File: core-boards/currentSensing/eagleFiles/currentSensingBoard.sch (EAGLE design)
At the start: 22 parts, among them Q1 16MHz, X1 3-PIN_2MM-H, X2 2-PIN_2MM-H, X3 4-PIN_2MM-H

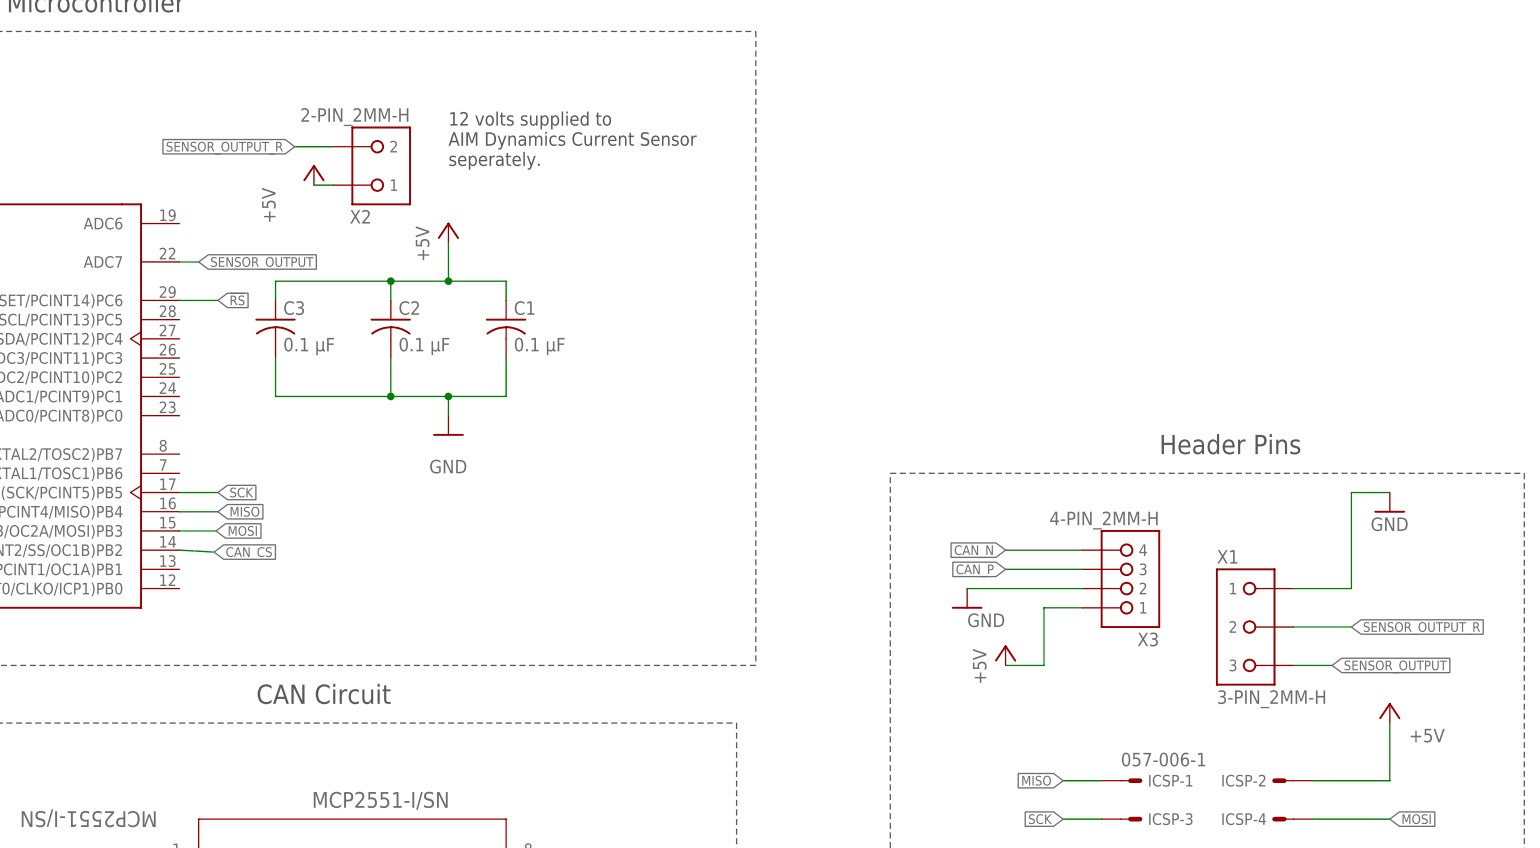
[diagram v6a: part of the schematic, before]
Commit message: SMD Resistor Update
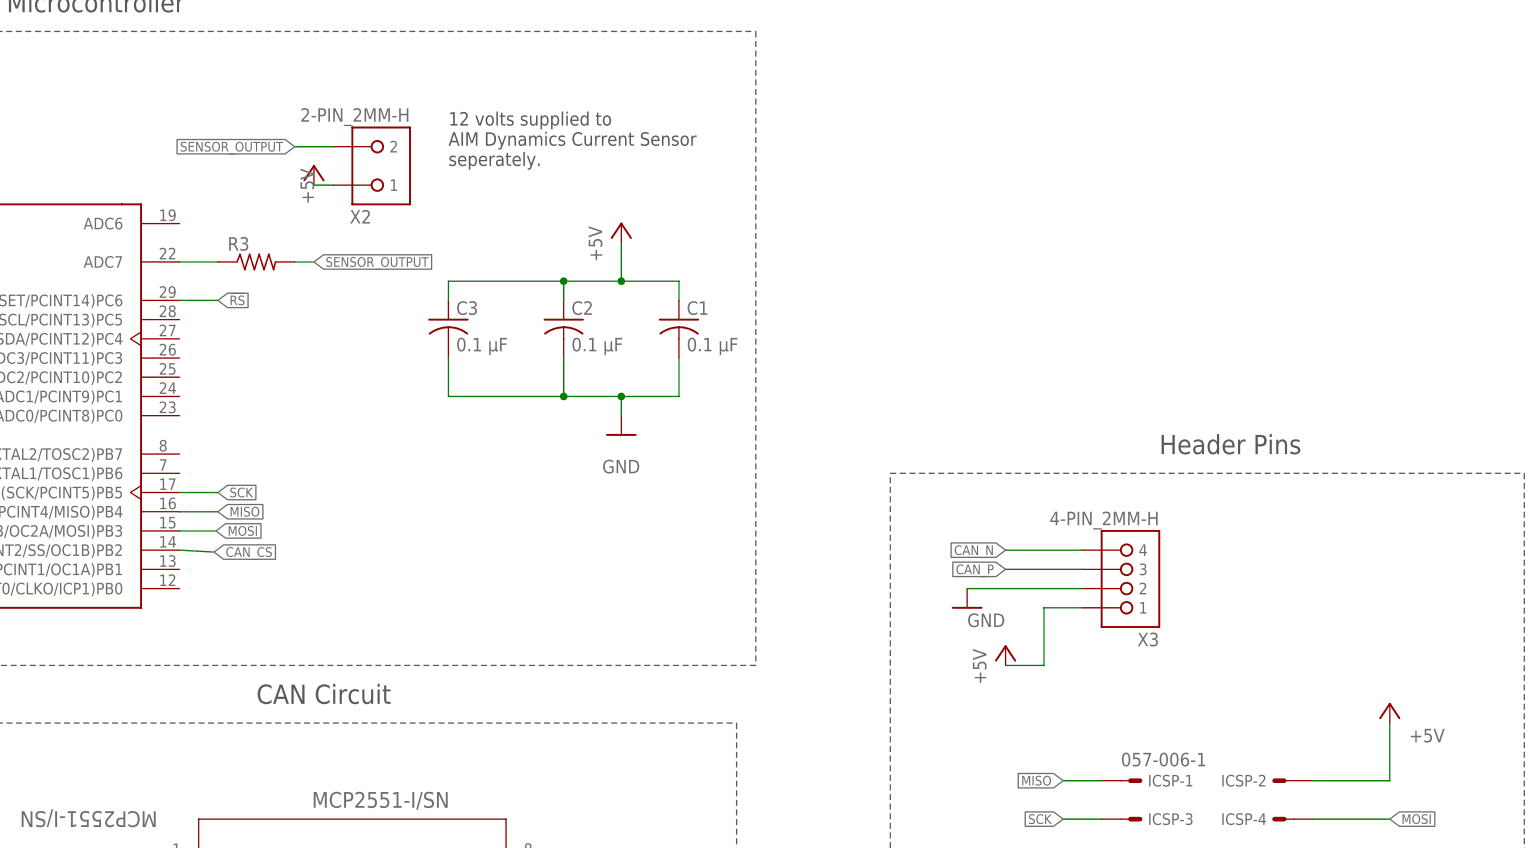
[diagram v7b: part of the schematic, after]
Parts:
- removed X1: 3-PIN_2MM-H, RoboJackets-Connectors:3-PIN_2MM-H
- added R3: (no value), RoboJackets-Resistors:R0603W
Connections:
- removed net SENSOR_OUTPUT_R: X1.2, X2.2
- new net N$2: ATMEGA328P-AU(V1).ADC7, R3.PIN1
- net GND: no longer X1.1
- net SENSOR_OUTPUT: now also R3.PIN2, X2.2; no longer ATMEGA328P-AU(V1).ADC7, X1.3
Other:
- moved on the sheet: C1, C2, C3
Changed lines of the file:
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@@
 <part name="R4" library="rcl" library_urn="urn:adsk.eagle:library:334" deviceset="R-US_" device="R0603" package3d_urn="urn:adsk.eagle:package:23555/3" value="120 Ω"/>
 <part name="R5" library="rcl" library_urn="urn:adsk.eagle:library:334" deviceset="R-US_" device="R0603" package3d_urn="urn:adsk.eagle:package:23555/3" value="120 Ω"/>
-<part name="X1" library="RoboJackets-Connectors" deviceset="3-PIN_2MM-*" device="H"/>
-<part name="GND5" library="supply1" library_urn="urn:adsk.eagle:library:371" deviceset="GND" device=""/>
 <part name="P+3" library="supply1" library_urn="urn:adsk.eagle:library:371" deviceset="+5V" device=""/>
 <part name="P+4" library="supply1" library_urn="urn:adsk.eagle:library:371" deviceset="+5V" device=""/>
@@
 <part name="DEBUG" library="RoboJackets-LEDs" deviceset="LED-SMD" device="" technology="-RED" value="RED"/>
 <part name="FRAME1" library="RoboJackets-Frames" deviceset="FRAME_B_L" device=""/>
+<part name="R3" library="RoboJackets-Resistors" deviceset="R0603W" device=""/>
 </parts>
 <sheets>
@@
 <attribute name="PARTS_NAME" x="147.32" y="215.9" size="1.778" layer="96"/>
 </instance>
-<instance part="C1" gate="G$1" x="233.68" y="198.12" smashed="yes">
-<attribute name="NAME" x="234.696" y="198.755" size="1.778" layer="95"/>
-<attribute name="VALUE" x="234.696" y="193.929" size="1.778" layer="96"/>
-</instance>
-<instance part="C2" gate="G$1" x="218.44" y="198.12" smashed="yes">
-<attribute name="NAME" x="219.456" y="198.755" size="1.778" layer="95"/>
-<attribute name="VALUE" x="219.456" y="193.929" size="1.778" layer="96"/>
-</instance>
-<instance part="P+1" gate="1" x="226.06" y="210.82" smashed="yes">
-<attribute name="VALUE" x="223.52" y="205.74" size="1.778" layer="96" rot="R90"/>
-</instance>
-<instance part="GND1" gate="1" x="226.06" y="182.88" smashed="yes">
-<attribute name="VALUE" x="223.52" y="177.8" size="1.778" layer="96"/>
+<instance part="C1" gate="G$1" x="256.54" y="198.12" smashed="yes">
+<attribute name="NAME" x="257.556" y="198.755" size="1.778" layer="95"/>
+<attribute name="VALUE" x="257.556" y="193.929" size="1.778" layer="96"/>
+</instance>
+<instance part="C2" gate="G$1" x="241.3" y="198.12" smashed="yes">
+<attribute name="NAME" x="242.316" y="198.755" size="1.778" layer="95"/>
+<attribute name="VALUE" x="242.316" y="193.929" size="1.778" layer="96"/>
+</instance>
+<instance part="P+1" gate="1" x="248.92" y="210.82" smashed="yes">
+<attribute name="VALUE" x="246.38" y="205.74" size="1.778" layer="96" rot="R90"/>
+</instance>
+<instance part="GND1" gate="1" x="248.92" y="182.88" smashed="yes">
+<attribute name="VALUE" x="246.38" y="177.8" size="1.778" layer="96"/>
 </instance>
 <instance part="GND2" gate="1" x="106.68" y="185.42" smashed="yes">
@@
 <attribute name="VALUE" x="254" y="119.38" size="1.778" layer="96"/>
 </instance>
-<instance part="C3" gate="G$1" x="203.2" y="198.12" smashed="yes">
-<attribute name="NAME" x="204.216" y="198.755" size="1.778" layer="95"/>
-<attribute name="VALUE" x="204.216" y="193.929" size="1.778" layer="96"/>
+<instance part="C3" gate="G$1" x="226.06" y="198.12" smashed="yes">
+<attribute name="NAME" x="227.076" y="198.755" size="1.778" layer="95"/>
+<attribute name="VALUE" x="227.076" y="193.929" size="1.778" layer="96"/>
 </instance>
 <instance part="C4" gate="G$1" x="116.84" y="187.96" smashed="yes" rot="R270">
@@
 <attribute name="VALUE" x="117.602" y="72.39" size="1.778" layer="96" rot="R90"/>
 </instance>
-<instance part="X1" gate="G$1" x="332.74" y="157.48" smashed="yes">
-<attribute name="NAME" x="327.66" y="167.64" size="1.778" layer="95" font="vector" align="top-left"/>
-<attribute name="VALUE" x="327.66" y="147.32" size="1.778" layer="96" font="vector"/>
-</instance>
-<instance part="GND5" gate="1" x="350.52" y="172.72" smashed="yes">
-<attribute name="VALUE" x="347.98" y="170.18" size="1.778" layer="96"/>
-</instance>
 <instance part="P+3" gate="1" x="101.6" y="218.44" smashed="yes">
 <attribute name="VALUE" x="99.06" y="213.36" size="1.778" layer="96" rot="R90"/>
@@
 </instance>
 <instance part="P+6" gate="1" x="208.28" y="218.44" smashed="yes">
-<attribute name="VALUE" x="203.2" y="210.82" size="1.778" layer="96" rot="R90"/>
+<attribute name="VALUE" x="208.28" y="213.36" size="1.778" layer="96" rot="R90"/>
 </instance>
 <instance part="GND7" gate="1" x="91.44" y="198.12" smashed="yes">
@@
 <attribute name="SCH_DESC" x="326.39" y="6.35" size="2.54" layer="94"/>
 </instance>
+<instance part="R3" gate="G$1" x="200.66" y="205.74" smashed="yes">
+<attribute name="NAME" x="196.85" y="207.2386" size="1.778" layer="95"/>
+<attribute name="VALUE" x="196.85" y="202.438" size="1.778" layer="96"/>
+</instance>
 </instances>
 <busses>
@@
 <segment>
 <pinref part="P+1" gate="1" pin="+5V"/>
-<wire x1="226.06" y1="208.28" x2="226.06" y2="203.2" width="0.1524" layer="91"/>
-<wire x1="226.06" y1="203.2" x2="233.68" y2="203.2" width="0.1524" layer="91"/>
+<wire x1="248.92" y1="208.28" x2="248.92" y2="203.2" width="0.1524" layer="91"/>
+<wire x1="248.92" y1="203.2" x2="256.54" y2="203.2" width="0.1524" layer="91"/>
 <pinref part="C1" gate="G$1" pin="1"/>
-<wire x1="233.68" y1="203.2" x2="233.68" y2="200.66" width="0.1524" layer="91"/>
-<wire x1="226.06" y1="203.2" x2="218.44" y2="203.2" width="0.1524" layer="91"/>
-<junction x="226.06" y="203.2"/>
+<wire x1="256.54" y1="203.2" x2="256.54" y2="200.66" width="0.1524" layer="91"/>
+<wire x1="248.92" y1="203.2" x2="241.3" y2="203.2" width="0.1524" layer="91"/>
+<junction x="248.92" y="203.2"/>
 <pinref part="C2" gate="G$1" pin="1"/>
-<wire x1="218.44" y1="203.2" x2="218.44" y2="200.66" width="0.1524" layer="91"/>
-<wire x1="218.44" y1="203.2" x2="203.2" y2="203.2" width="0.1524" layer="91"/>
-<junction x="218.44" y="203.2"/>
+<wire x1="241.3" y1="203.2" x2="241.3" y2="200.66" width="0.1524" layer="91"/>
+<wire x1="241.3" y1="203.2" x2="226.06" y2="203.2" width="0.1524" layer="91"/>
+<junction x="241.3" y="203.2"/>
 <pinref part="C3" gate="G$1" pin="1"/>
-<wire x1="203.2" y1="203.2" x2="203.2" y2="200.66" width="0.1524" layer="91"/>
+<wire x1="226.06" y1="203.2" x2="226.06" y2="200.66" width="0.1524" layer="91"/>
 </segment>
 <segment>
@@
 <segment>
 <pinref part="C2" gate="G$1" pin="2"/>
-<wire x1="218.44" y1="193.04" x2="218.44" y2="187.96" width="0.1524" layer="91"/>
-<wire x1="218.44" y1="187.96" x2="226.06" y2="187.96" width="0.1524" layer="91"/>
+<wire x1="241.3" y1="193.04" x2="241.3" y2="187.96" width="0.1524" layer="91"/>
+<wire x1="241.3" y1="187.96" x2="248.92" y2="187.96" width="0.1524" layer="91"/>
 <pinref part="GND1" gate="1" pin="GND"/>
-<wire x1="226.06" y1="187.96" x2="226.06" y2="185.42" width="0.1524" layer="91"/>
-<wire x1="226.06" y1="187.96" x2="233.68" y2="187.96" width="0.1524" layer="91"/>
-<junction x="226.06" y="187.96"/>
+<wire x1="248.92" y1="187.96" x2="248.92" y2="185.42" width="0.1524" layer="91"/>
+<wire x1="248.92" y1="187.96" x2="256.54" y2="187.96" width="0.1524" layer="91"/>
+<junction x="248.92" y="187.96"/>
 <pinref part="C1" gate="G$1" pin="2"/>
-<wire x1="233.68" y1="187.96" x2="233.68" y2="193.04" width="0.1524" layer="91"/>
+<wire x1="256.54" y1="187.96" x2="256.54" y2="193.04" width="0.1524" layer="91"/>
 <pinref part="C3" gate="G$1" pin="2"/>
-<wire x1="203.2" y1="193.04" x2="203.2" y2="187.96" width="0.1524" layer="91"/>
-<wire x1="203.2" y1="187.96" x2="218.44" y2="187.96" width="0.1524" layer="91"/>
-<junction x="218.44" y="187.96"/>
+<wire x1="226.06" y1="193.04" x2="226.06" y2="187.96" width="0.1524" layer="91"/>
+<wire x1="226.06" y1="187.96" x2="241.3" y2="187.96" width="0.1524" layer="91"/>
+<junction x="241.3" y="187.96"/>
 </segment>
 <segment>
@@
 <pinref part="C4" gate="G$1" pin="2"/>
 <wire x1="111.76" y1="187.96" x2="106.68" y2="187.96" width="0.1524" layer="91"/>
-</segment>
-<segment>
-<pinref part="X1" gate="G$1" pin="1"/>
-<wire x1="337.82" y1="162.56" x2="345.44" y2="162.56" width="0.1524" layer="91"/>
-<pinref part="GND5" gate="1" pin="GND"/>
-<wire x1="345.44" y1="162.56" x2="345.44" y2="175.26" width="0.1524" layer="91"/>
-<wire x1="345.44" y1="175.26" x2="350.52" y2="175.26" width="0.1524" layer="91"/>
 </segment>
 <segment>
@@
 <net name="SENSOR_OUTPUT" class="0">
 <segment>
-<pinref part="X1" gate="G$1" pin="3"/>
-<wire x1="337.82" y1="152.4" x2="342.9" y2="152.4" width="0.1524" layer="91"/>
-<label x="342.9" y="152.4" size="1.27" layer="95" font="vector" xref="yes"/>
-</segment>
-<segment>
-<pinref part="ATMEGA328P-AU(V1)" gate="G$1" pin="ADC7"/>
-<wire x1="193.04" y1="205.74" x2="190.5" y2="205.74" width="0.1524" layer="91"/>
-<label x="193.04" y="205.74" size="1.27" layer="95" xref="yes"/>
+<pinref part="X2" gate="G$1" pin="2"/>
+<wire x1="210.82" y1="220.98" x2="205.74" y2="220.98" width="0.1524" layer="91"/>
+<label x="205.74" y="220.98" size="1.27" layer="95" rot="R180" xref="yes"/>
+</segment>
+<segment>
+<pinref part="R3" gate="G$1" pin="PIN2"/>
+<wire x1="205.74" y1="205.74" x2="208.28" y2="205.74" width="0.1524" layer="91"/>
+<label x="208.28" y="205.74" size="1.27" layer="95" xref="yes"/>
 </segment>
 </net>
@@
 </segment>
 </net>
-<net name="SENSOR_OUTPUT_R" class="0">
-<segment>
-<pinref part="X2" gate="G$1" pin="2"/>
-<wire x1="210.82" y1="220.98" x2="205.74" y2="220.98" width="0.1524" layer="91"/>
-<label x="205.74" y="220.98" size="1.27" layer="95" rot="R180" xref="yes"/>
-</segment>
-<segment>
-<pinref part="X1" gate="G$1" pin="2"/>
-<wire x1="337.82" y1="157.48" x2="345.44" y2="157.48" width="0.1524" layer="91"/>
-<label x="345.44" y="157.48" size="1.27" layer="95" xref="yes"/>
-</segment>
-</net>
+<net name="N$2" class="0">
+<segment>
+<pinref part="ATMEGA328P-AU(V1)" gate="G$1" pin="ADC7"/>
+<pinref part="R3" gate="G$1" pin="PIN1"/>
+<wire x1="190.5" y1="205.74" x2="195.58" y2="205.74" width="0.1524" layer="91"/>
+</segment>
+</net>
